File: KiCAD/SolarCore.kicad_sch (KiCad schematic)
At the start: 15 parts, among them U1 LMR33630ARNXR

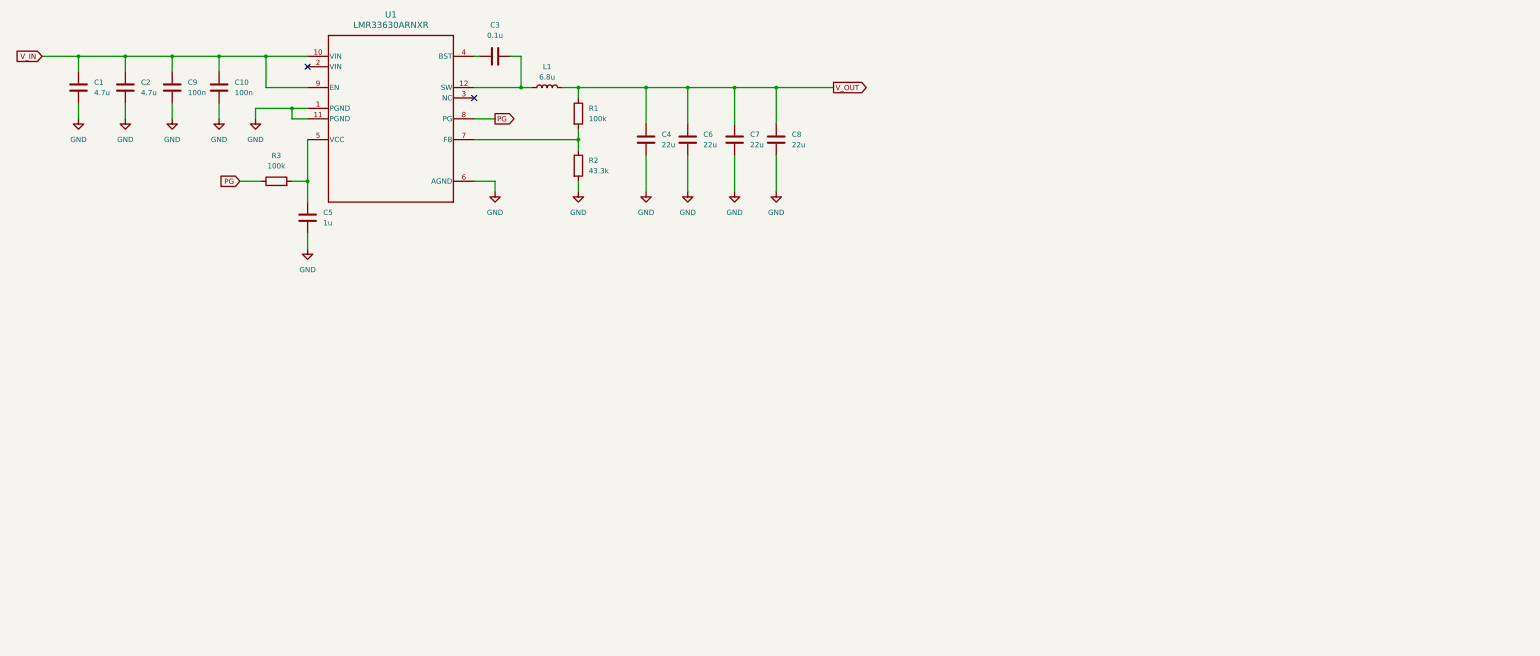
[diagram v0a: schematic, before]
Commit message: Project reorganization
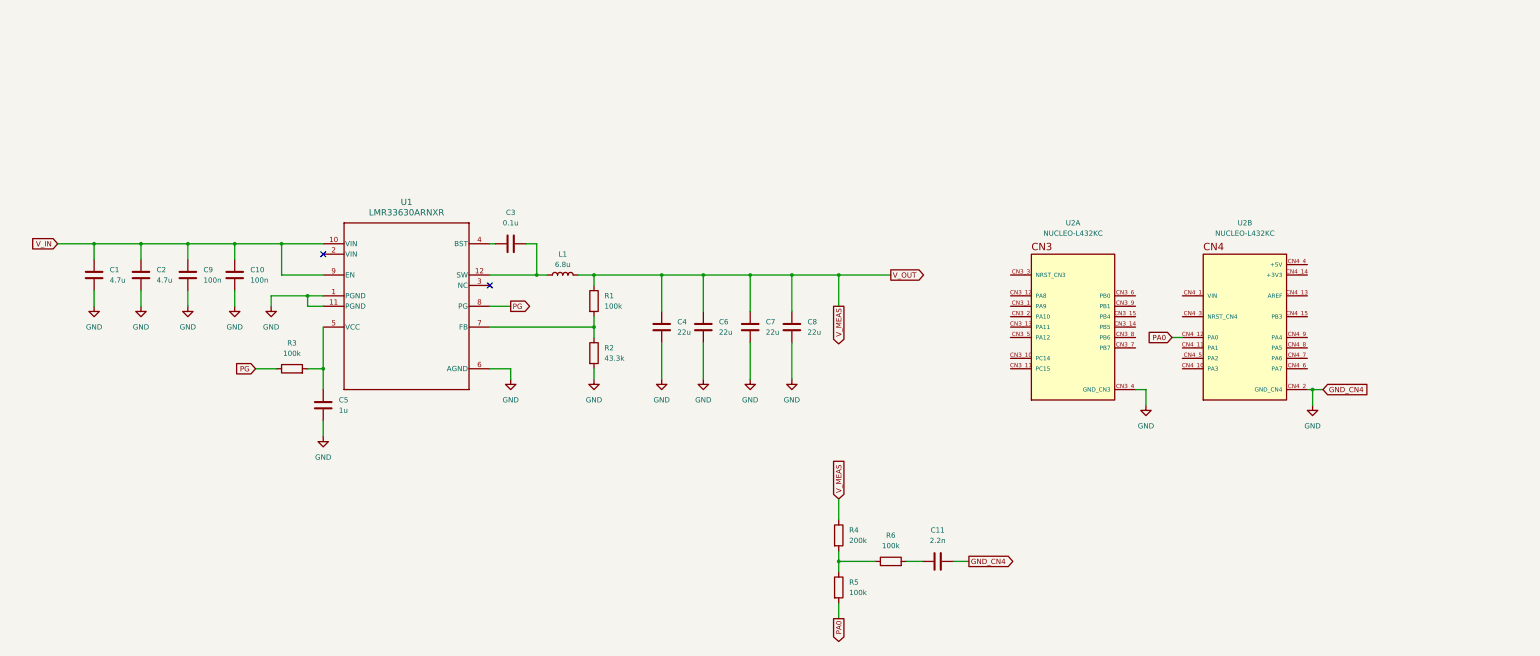
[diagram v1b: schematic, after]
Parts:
- added C11: 2.2n, symbol Device:C
- added R4: 200k, symbol Device:R
- added R5, R6: 100k, symbol Device:R
- added U2: NUCLEO-L432KC, NUCLEO-L432KC:MODULE_NUCLEO-L432KC, symbol NUCLEO-L432KC:NUCLEO-L432KC
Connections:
- net GND: now also C11.2, U2.CN3_4 (GND_CN3), U2.CN4_2 (GND_CN4)
- net V_OUT renamed V_MEAS
- net V_MEAS: now also R4.1
- new net: R4.2, R5.1, R6.1
- new net: C11.1, R6.2
- new net PA0: R5.2, U2.CN4_12 (PA0)
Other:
- moved on the sheet: C1, C10, C2, C3, C4, C5, C6, C7, C8, C9, L1, R1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

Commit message: Input voltage measure
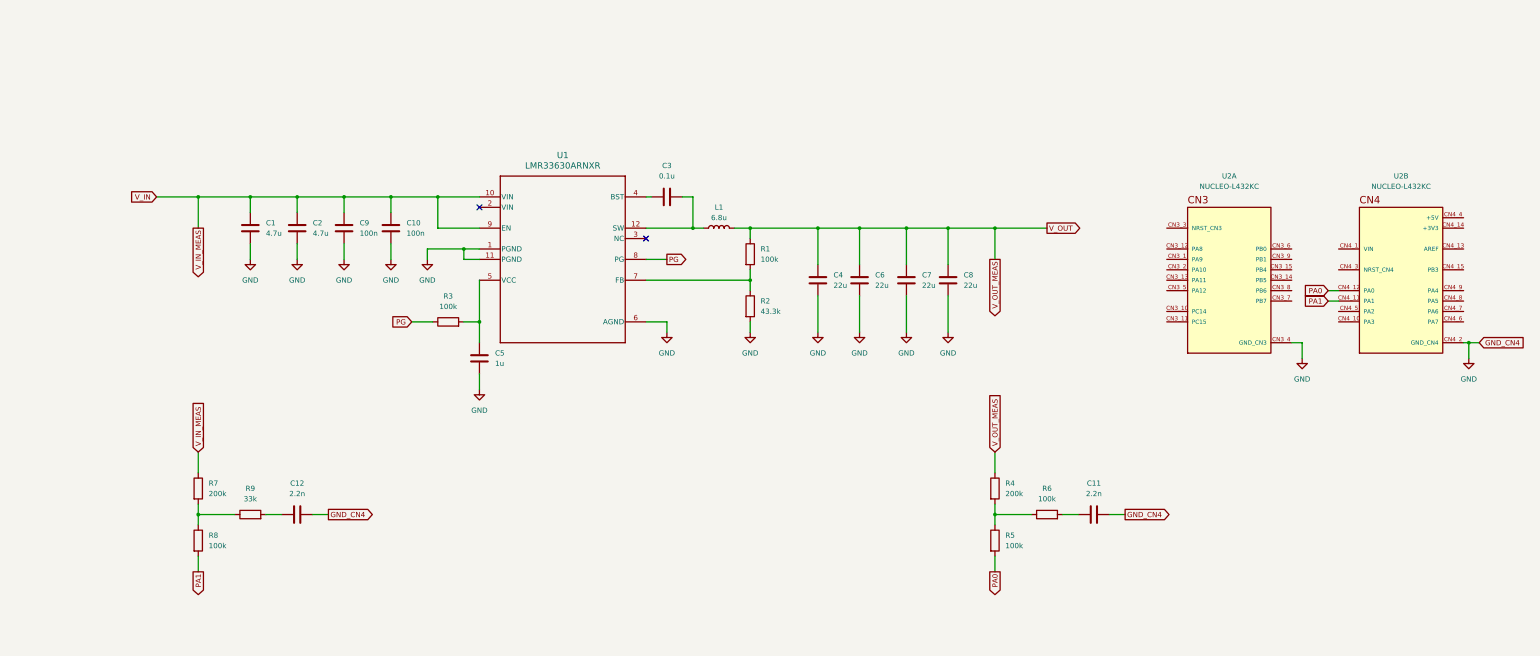
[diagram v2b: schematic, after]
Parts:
- added C12: 2.2n, symbol Device:C
- added R7: 200k, symbol Device:R
- added R8: 100k, symbol Device:R
- added R9: 33k, symbol Device:R
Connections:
- net GND: now also C12.2
- net V_IN: now also R7.1
- net PA1: now reaches U2.CN4_11 (PA1)
- net PA1: now also R8.2
- net V_MEAS renamed V_OUT
- new net: R7.2, R8.1, R9.1
- new net: C12.1, R9.2
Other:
- moved on the sheet: C1, C10, C11, C2, C3, C4, C5, C6, C7, C8, C9, L1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

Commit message: Add footprints
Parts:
- C1, C10, C2, C4, C6, C7, C8, C9: footprint (none) -> Capacitor_SMD:CP_Elec_4x5.4
- C11, C12, C3, C5: footprint (none) -> Capacitor_SMD:C_0603_1608Metric_Pad1.08x0.95mm_HandSolder
- L1: footprint (none) -> Inductor_SMD:L_Coilcraft_XAL5030-XXX
- R1, R2, R3, R4, R5, R6, R7, R8, R9: footprint (none) -> Resistor_SMD:R_0603_1608Metric_Pad0.98x0.95mm_HandSolder
- U1: footprint RNX0012B -> footprints:RNX0012B
- U2: footprint NUCLEO-L432KC:MODULE_NUCLEO-L432KC -> NUCLEO_L432KC:MODULE_NUCLEO-L432KC
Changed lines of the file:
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@@
 			)
 		)
-		(property "Footprint" ""
+		(property "Footprint" "Resistor_SMD:R_0603_1608Metric_Pad0.98x0.95mm_HandSolder"
 			(at 81.28 184.658 90)
 			(effects
@@
 			)
 		)
-		(property "Footprint" ""
+		(property "Footprint" "Resistor_SMD:R_0603_1608Metric_Pad0.98x0.95mm_HandSolder"
 			(at 261.112 176.53 90)
 			(effects
@@
 			)
 		)
-		(property "Footprint" ""
+		(property "Footprint" "Capacitor_SMD:CP_Elec_4x5.4"
 			(at 228.9048 121.92 0)
 			(effects
@@
 			)
 		)
-		(property "Footprint" ""
+		(property "Footprint" "Capacitor_SMD:CP_Elec_4x5.4"
 			(at 82.2452 116.84 0)
 			(effects
@@
 			)
 		)
-		(property "Footprint" ""
+		(property "Footprint" "Capacitor_SMD:CP_Elec_4x5.4"
 			(at 116.5352 116.84 0)
 			(effects
@@
 			)
 		)
-		(property "Footprint" ""
+		(property "Footprint" "Capacitor_SMD:CP_Elec_4x5.4"
 			(at 218.7448 121.92 0)
 			(effects
@@
 			)
 		)
-		(property "Footprint" ""
+		(property "Footprint" "Resistor_SMD:R_0603_1608Metric_Pad0.98x0.95mm_HandSolder"
 			(at 275.59 184.658 90)
 			(effects
@@
 			)
 		)
-		(property "Footprint" ""
+		(property "Footprint" "Capacitor_SMD:C_0603_1608Metric_Pad1.08x0.95mm_HandSolder"
 			(at 138.1252 148.59 0)
 			(effects
@@
 			)
 		)
-		(property "Footprint" ""
+		(property "Footprint" "Capacitor_SMD:C_0603_1608Metric_Pad1.08x0.95mm_HandSolder"
 			(at 290.83 181.9148 0)
 			(effects
@@
 			)
 		)
-		(property "Footprint" ""
+		(property "Footprint" "Resistor_SMD:R_0603_1608Metric_Pad0.98x0.95mm_HandSolder"
 			(at 201.422 132.08 90)
 			(effects
@@
 			)
 		)
-		(property "Footprint" ""
+		(property "Footprint" "Capacitor_SMD:CP_Elec_4x5.4"
 			(at 240.3348 121.92 0)
 			(effects
@@
 			)
 		)
-		(property "Footprint" "NUCLEO-L432KC:MODULE_NUCLEO-L432KC"
+		(property "Footprint" "NUCLEO_L432KC:MODULE_NUCLEO-L432KC"
 			(at 361.95 125.73 0)
 			(effects
@@
 			)
 		)
-		(property "Footprint" ""
+		(property "Footprint" "Resistor_SMD:R_0603_1608Metric_Pad0.98x0.95mm_HandSolder"
 			(at 201.422 119.38 90)
 			(effects
@@
 			)
 		)
-		(property "Footprint" ""
+		(property "Footprint" "Resistor_SMD:R_0603_1608Metric_Pad0.98x0.95mm_HandSolder"
 			(at 66.802 189.23 90)
 			(effects
@@
 			)
 		)
-		(property "Footprint" "RNX0012B"
+		(property "Footprint" "footprints:RNX0012B"
 			(at 157.48 120.65 0)
 			(effects
@@
 			)
 		)
-		(property "Footprint" ""
+		(property "Footprint" "Resistor_SMD:R_0603_1608Metric_Pad0.98x0.95mm_HandSolder"
 			(at 129.54 137.668 90)
 			(effects
@@
 			)
 		)
-		(property "Footprint" ""
+		(property "Footprint" "Resistor_SMD:R_0603_1608Metric_Pad0.98x0.95mm_HandSolder"
 			(at 261.112 189.23 90)
 			(effects
@@
 			)
 		)
-		(property "Footprint" ""
+		(property "Footprint" "Capacitor_SMD:C_0603_1608Metric_Pad1.08x0.95mm_HandSolder"
 			(at 96.52 181.9148 0)
 			(effects
@@
 			)
 		)
-		(property "Footprint" ""
+		(property "Footprint" "Inductor_SMD:L_Coilcraft_XAL5030-XXX"
 			(at 195.58 113.03 0)
 			(effects
@@
 			)
 		)
-		(property "Footprint" ""
+		(property "Footprint" "Capacitor_SMD:CP_Elec_4x5.4"
 			(at 93.6752 116.84 0)
 			(effects
@@
 			)
 		)
-		(property "Footprint" ""
+		(property "Footprint" "Capacitor_SMD:C_0603_1608Metric_Pad1.08x0.95mm_HandSolder"
 			(at 186.69 104.4448 0)
 			(effects
@@
 			)
 		)
-		(property "Footprint" ""
+		(property "Footprint" "Capacitor_SMD:CP_Elec_4x5.4"
 			(at 250.4948 121.92 0)
 			(effects
@@
 			)
 		)
-		(property "Footprint" ""
+		(property "Footprint" "Capacitor_SMD:CP_Elec_4x5.4"
 			(at 105.1052 116.84 0)
 			(effects
@@
 			)
 		)
-		(property "Footprint" "NUCLEO-L432KC:MODULE_NUCLEO-L432KC"
+		(property "Footprint" "NUCLEO_L432KC:MODULE_NUCLEO-L432KC"
 			(at 320.04 125.73 0)
 			(effects
@@
 			)
 		)
-		(property "Footprint" ""
+		(property "Footprint" "Resistor_SMD:R_0603_1608Metric_Pad0.98x0.95mm_HandSolder"
 			(at 66.802 176.53 90)
 			(effects

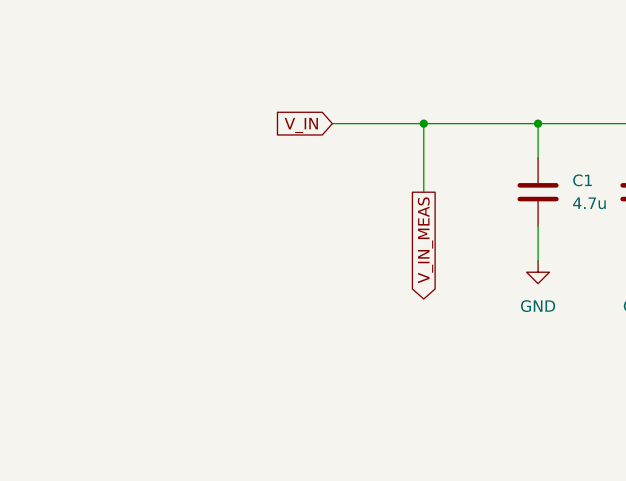
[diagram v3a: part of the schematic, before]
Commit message: Increasing circuit safety
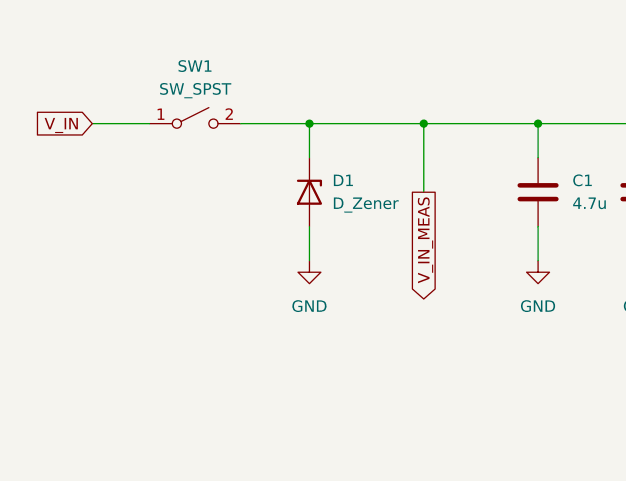
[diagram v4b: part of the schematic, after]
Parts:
- added D1: D_Zener, Diode_SMD:D_SMB-SMC_Universal_Handsoldering, symbol Device:D_Zener
- added SW1: SW_SPST, symbol Switch:SW_SPST
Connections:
- net GND: now also D1.2 (A)
- net V_IN: now also SW1.1 (A); no longer C1.1, C10.1, C2.1, C9.1, R7.1, U1.10 (VIN), U1.9 (EN)
- new net V_IN_MEAS: C1.1, C10.1, C2.1, C9.1, D1.1 (K), R7.1, SW1.2 (B), U1.10 (VIN), U1.9 (EN)

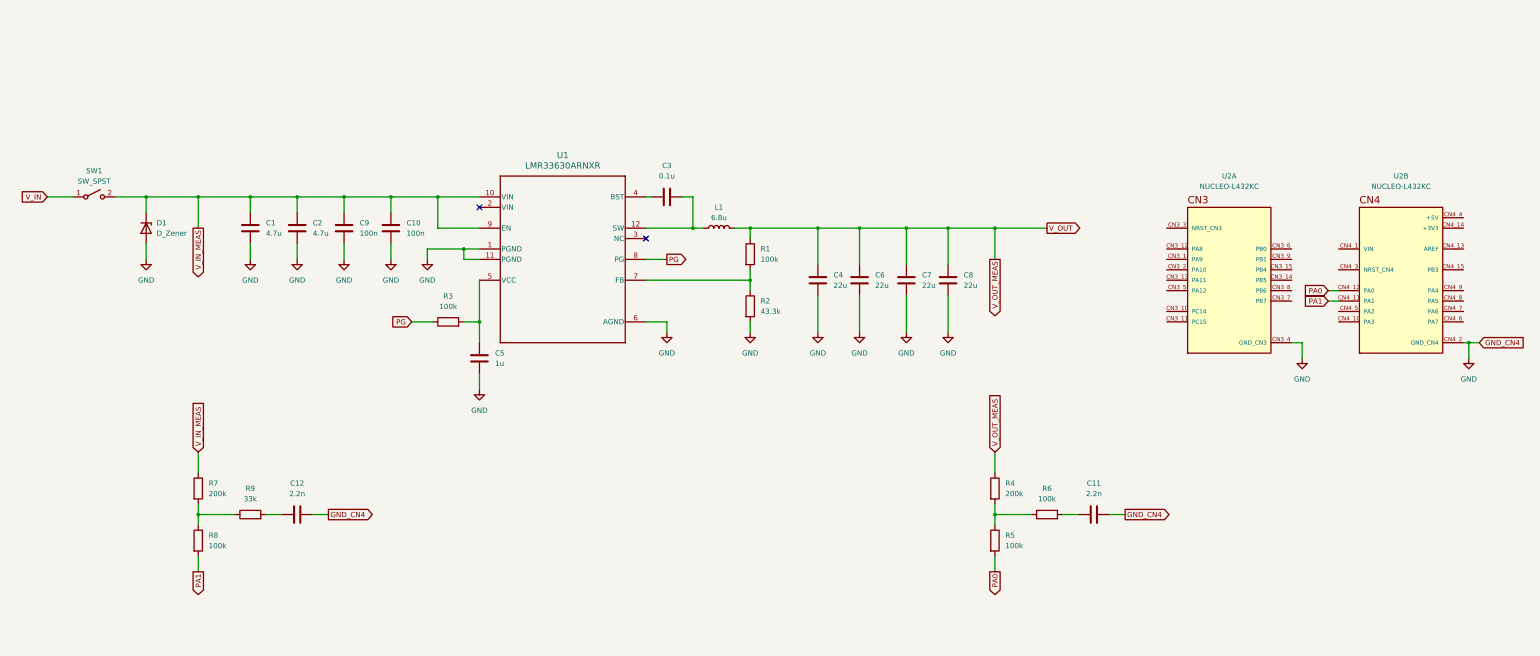
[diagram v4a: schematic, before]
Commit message: First version of the schematic
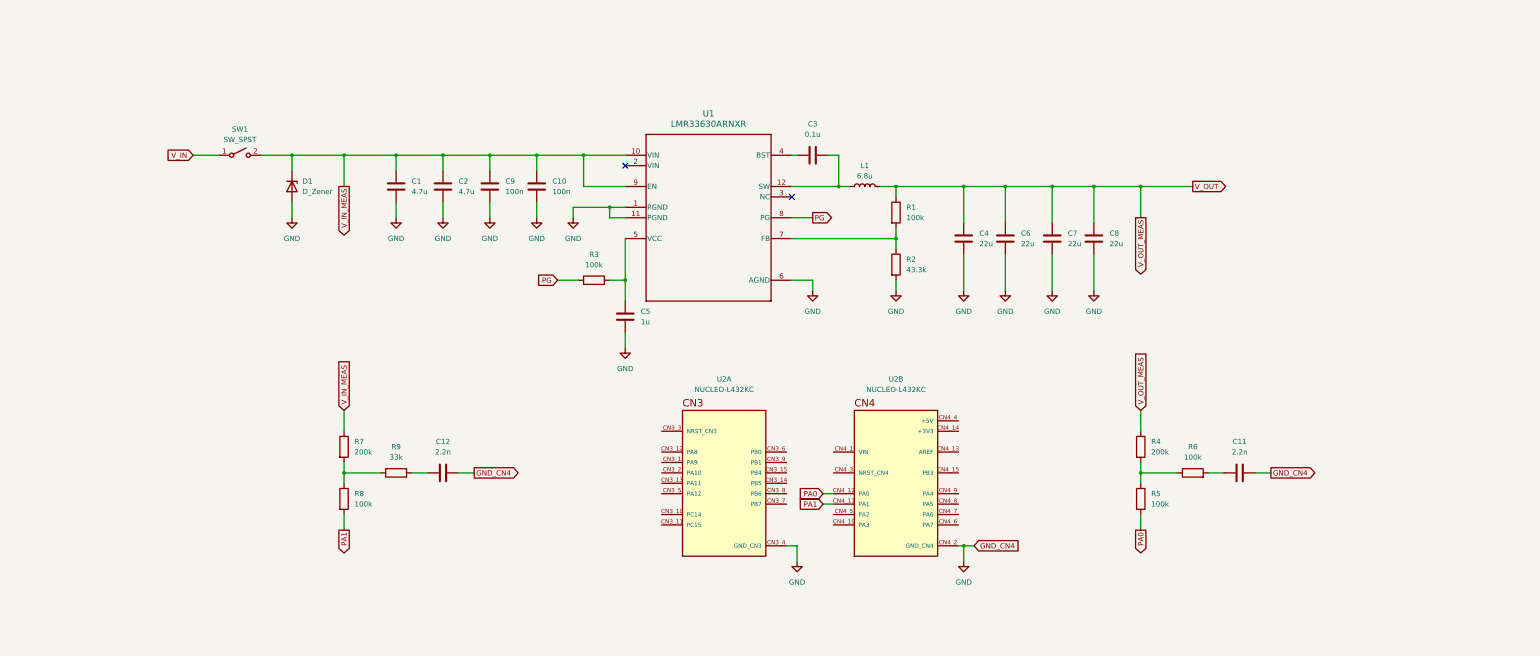
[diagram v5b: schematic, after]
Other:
- company: (none) -> Mateusz Witczak
- title: (none) -> SolarCore
- moved on the sheet: C1, C10, C11, C12, C2, C3, C4, C5, C6, C7, C8, C9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

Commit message: Final schematic V1
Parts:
- added F1: Fuse, Fuse:Fuse_2512_6332Metric_Pad1.52x3.35mm_HandSolder, symbol Device:Fuse
- SW1: footprint (none) -> Connector_JST:JST_VH_B2P-VH_1x02_P3.96mm_Vertical
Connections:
- net V_IN: no longer names the net of SW1.1 (A)
- net V_IN: now also F1.2
- net V_OUT renamed V_OUT+
- new net V_IN+: F1.1
- no-connect marks 2 -> 28
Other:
- moved on the sheet: C1, C10, C2, C4, C6, C7, C8, C9, D1, R3, SW1

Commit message: Final schematic V2
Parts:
- added J1: Conn_01x02_MountingPin, 282857-2:TE_282857-2, symbol Connector_Generic_MountingPin:Conn_01x02_MountingPin
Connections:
- net GND: now also U1.3 (NC), J1.2 (Pin_2)
- net V_IN+: no longer names the net of F1.1
- net V_IN+: now also J1.1 (Pin_1)

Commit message: Final schematic V3
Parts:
- added J2: Conn_01x02_MountingPin, Connector_JST:JST_VH_B2P-VH_1x02_P3.96mm_Vertical, symbol Connector_Generic_MountingPin:Conn_01x02_MountingPin
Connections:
- net GND: now also J2.2 (Pin_2)
- net V_OUT+ renamed V_OUT_MEAS
- net V_OUT_MEAS: now also J2.1 (Pin_1)
- no-connect marks 28 -> 29
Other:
- moved on the sheet: C1, C10, C11, C12, C2, C3, C4, C5, C6, C7, C8, C9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
